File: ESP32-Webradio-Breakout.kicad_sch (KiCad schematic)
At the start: 38 parts, among them J1 Conn_01x02, J2 RCJ-041, J3 RCJ-042, J4 Conn_01x02, Q1 BC547, SW1 RotaryEncoder_Switch, U1 TSR_1-2450, U2 ESP32NodeMCU, U3 PCF8574, U4 DS18B20

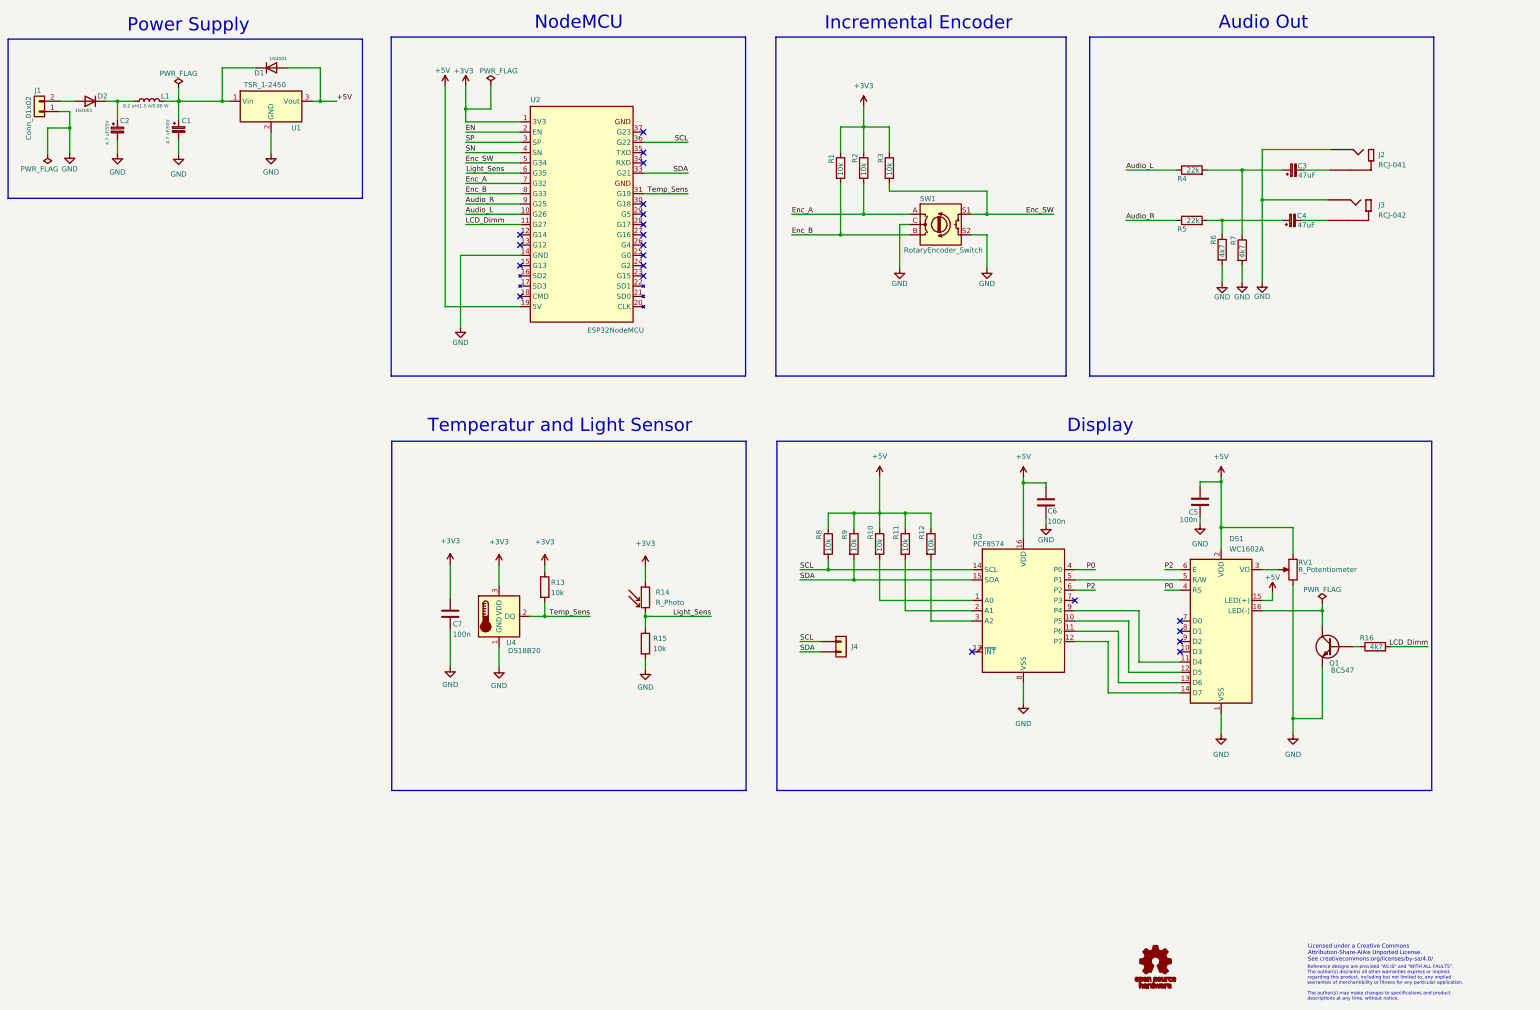
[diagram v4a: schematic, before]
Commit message: Added electrolytic capacitor to 5V line
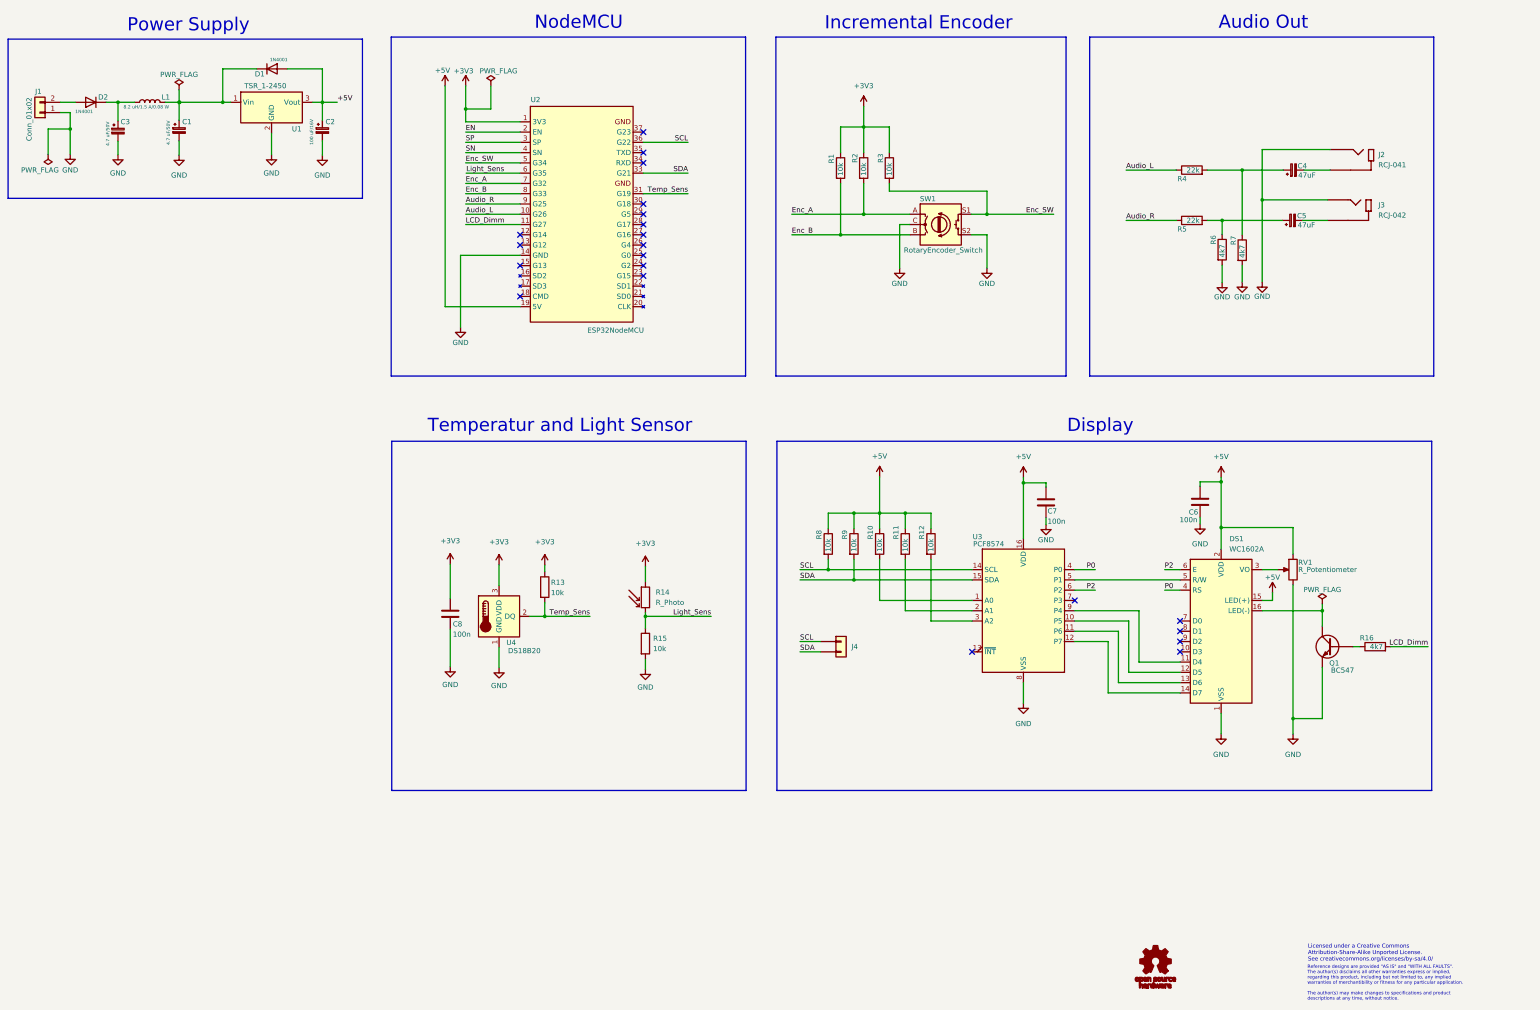
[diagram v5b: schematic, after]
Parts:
- added C2: 100 uF/16V, Capacitor_THT:CP_Radial_D6.3mm_P2.50mm, symbol Device:C_Polarized_Small
- renumbered C2 to C3, C3 to C4, C4 to C5, C5 to C6, C6 to C7, C7 to C8
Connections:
- net +5V: now also C2.1
- net GND: now also C2.2

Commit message: Parts placement Updated README Updated Images
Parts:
- DS1: footprint Display:WC1602A -> Connector_PinHeader_2.54mm:PinHeader_1x16_P2.54mm_Vertical
- L1: footprint Inductor_SMD:L_AVX_LMLP07A7 -> Inductor_THT:L_Axial_L14.5mm_D5.8mm_P20.32mm_Horizontal_Fastron_HBCC
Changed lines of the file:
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@@
       (effects (font (size 1.27 1.27)) (justify left))
     )
-    (property "Footprint" "Display:WC1602A" (id 2) (at 341.63 199.39 0)
+    (property "Footprint" "Connector_PinHeader_2.54mm:PinHeader_1x16_P2.54mm_Vertical" (id 2) (at 341.63 199.39 0)
       (effects (font (size 1.27 1.27) italic) hide)
     )
@@
       (effects (font (size 0.8128 0.8128)))
     )
-    (property "Footprint" "Inductor_SMD:L_AVX_LMLP07A7" (id 2) (at 76.708 45.72 0)
+    (property "Footprint" "Inductor_THT:L_Axial_L14.5mm_D5.8mm_P20.32mm_Horizontal_Fastron_HBCC" (id 2) (at 76.708 45.72 0)
       (effects (font (size 1.27 1.27)) hide)
     )
@@
     )
     (path "/031eb1d7-d1d9-4f4b-983d-0672a0b9b149"
-      (reference "DS1") (unit 1) (value "WC1602A") (footprint "Display:WC1602A")
+      (reference "DS1") (unit 1) (value "WC1602A") (footprint "Connector_PinHeader_2.54mm:PinHeader_1x16_P2.54mm_Vertical")
     )
     (path "/de588ed9-a530-46f0-aa03-e0307ff72286"
@@
     )
     (path "/6f462a43-fddc-4a67-950c-ae5029d95ab6"
-      (reference "L1") (unit 1) (value " 8.2 uH/1.5 A/0.08 W") (footprint "Inductor_SMD:L_AVX_LMLP07A7")
+      (reference "L1") (unit 1) (value " 8.2 uH/1.5 A/0.08 W") (footprint "Inductor_THT:L_Axial_L14.5mm_D5.8mm_P20.32mm_Horizontal_Fastron_HBCC")
     )
     (path "/aebcee85-771a-411d-bbca-6bc46bbc6b26"

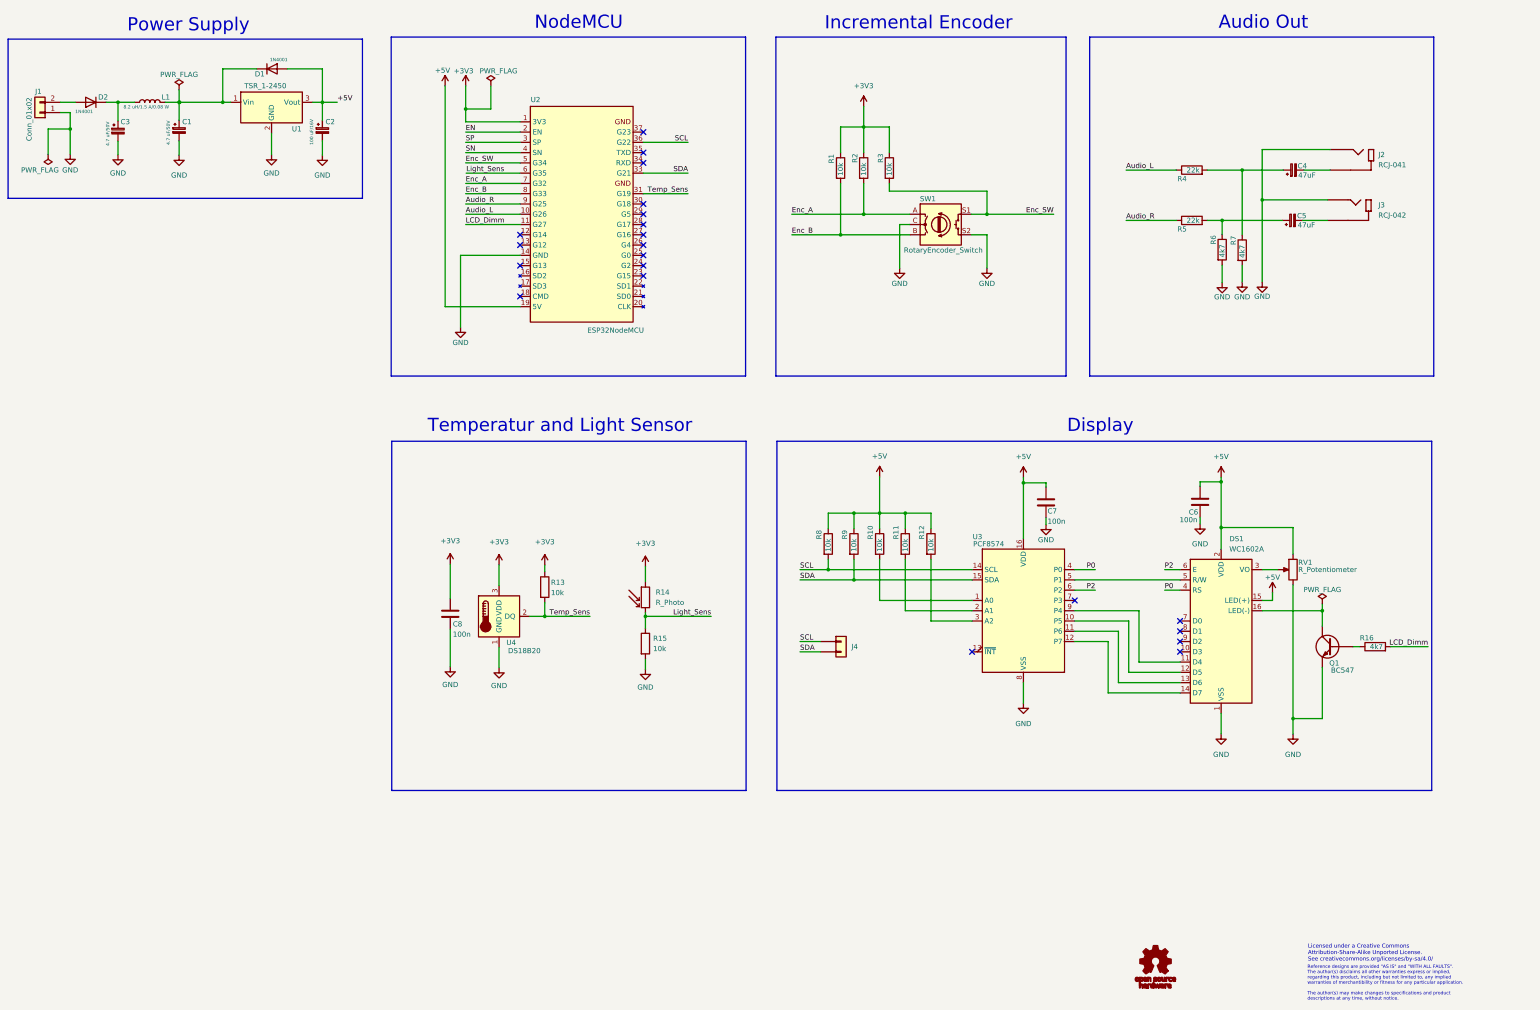
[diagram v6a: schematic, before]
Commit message: Removed 24V supply
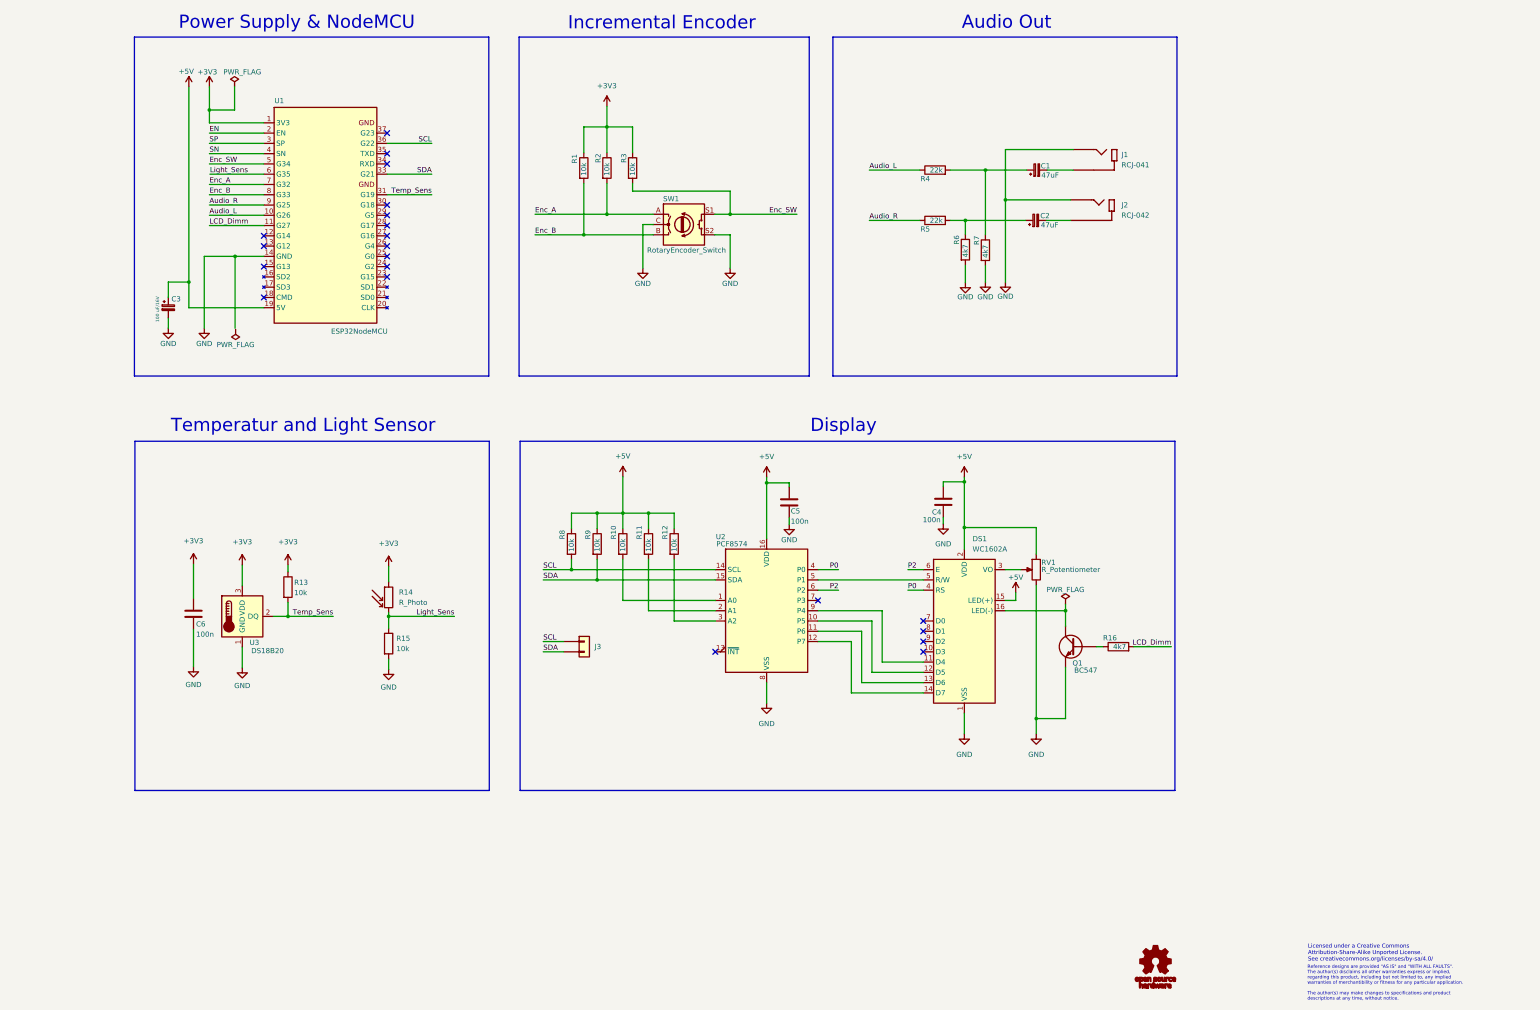
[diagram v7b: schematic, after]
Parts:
- removed C1, C3: 4.7 uF/50V, Capacitor_THT:CP_Radial_D6.3mm_P2.50mm, symbol Device:C_Polarized_Small
- removed D1, D2: 1N4001, Diode_THT:D_DO-41_SOD81_P10.16mm_Horizontal, symbol Diode:1N4001
- removed J1: Conn_01x02, TerminalBlock_RND:TerminalBlock_RND_205-00287_1x02_P5.08mm_Horizontal, symbol Connector_Generic:Conn_01x02
- removed L1: 8.2 uH/1.5 A/0.08 W, Inductor_THT:L_Axial_L14.5mm_D5.8mm_P20.32mm_Horizontal_Fastron_HBCC, symbol Device:L
- removed U1: TSR_1-2450, Converter_DCDC:Converter_DCDC_TRACO_TSR-1_THT, symbol Regulator_Switching:TSR_1-2450
- renumbered C4 to C1, C5 to C2, C2 to C3, C6 to C4, C7 to C5, C8 to C6, J2 to J1, J3 to J2, J4 to J3, U2 to U1, U3 to U2, U4 to U3
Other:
- note added: "Power Supply & NodeMCU"
- note removed: "NodeMCU"
- note removed: "Power Supply"
- moved on the sheet: C1, C2, C3, C4, C5, C6, DS1, J1, J2, J3, Q1, R1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

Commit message: Replaced Cinch Jacks by 3.5mm Jack New parts placement
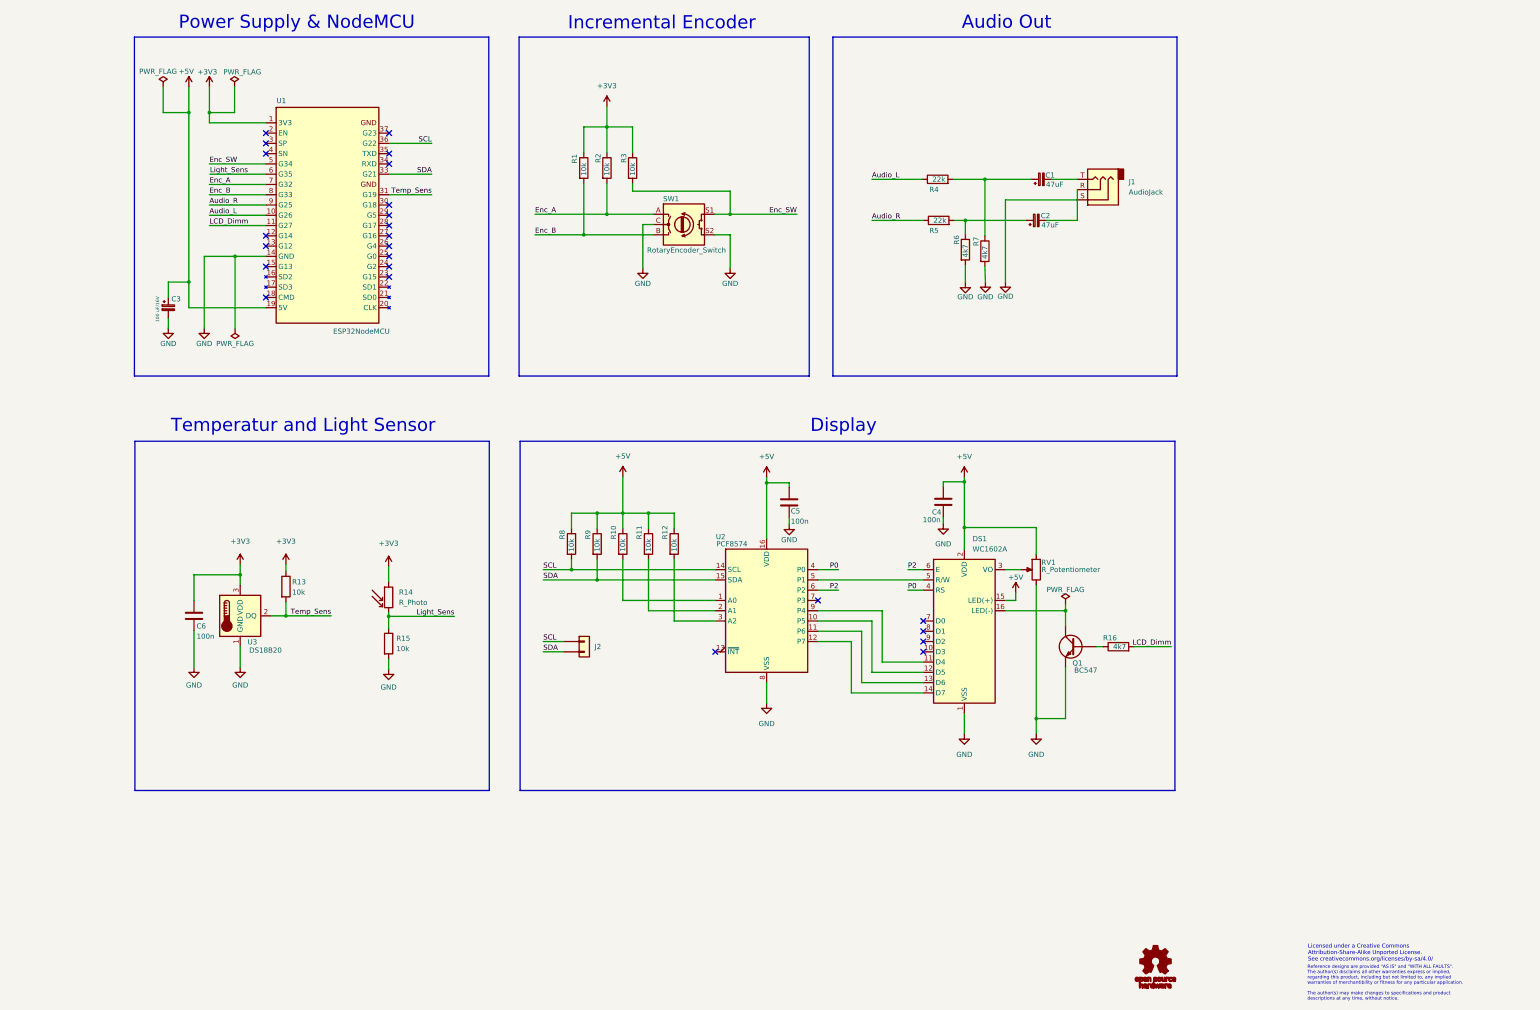
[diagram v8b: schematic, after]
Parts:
- removed J1: RCJ-041, RCJ-041:CUI_RCJ-041, symbol RCJ-041:RCJ-041
- removed J2: RCJ-042, RCJ-042:CUI_RCJ-042, symbol RCJ-042:RCJ-042
- added J1: AudioJack, Connector_Audio:Jack_3.5mm_CUI_SJ1-3533NG_Horizontal, symbol Connector:AudioJack3
- J2: renamed from J3; footprint TestPoint:TestPoint_2Pads_Pitch2.54mm_Drill0.8mm -> Connector_PinHeader_2.54mm:PinHeader_1x02_P2.54mm_Vertical
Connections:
- net GND: now also J1.S
- net at C1.2: now also J1.T
- net at C2.2: now also J1.R
- net EN: no longer names the net of U1.2 (EN)
- net SN: no longer names the net of U1.4 (SN)
- net SP: no longer names the net of U1.3 (SP)
- no-connect marks 21 -> 24
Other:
- moved on the sheet: C1, C6, R13, R4, R5, U1, U3
